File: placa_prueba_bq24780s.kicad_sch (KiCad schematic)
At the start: 1 part, among them U1 BQ24780SRUYR

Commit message: Avances en el esquemático.
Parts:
- added C22: 0.01u, symbol Device:C_Small
- added C3, C4, C5: 0.1u, symbol Device:C_Small
- added C6: 1u, symbol Device:C_Small
- added R20: 100k, symbol Device:R_Small
- added R21: 316k, symbol Device:R_Small
- added R7: 10, symbol Device:R_Small
- added RAC: 10m, symbol Device:R_Small
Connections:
- net at U1.1 (ACN): now also C4.1, C5.2, RAC.2
- net at U1.2 (ACP): now also C3.2, C4.2, RAC.1
- net at U1.21 (ILIM): now also C22.1, R20.1, R21.2
- net at U1.28 (VCC): now also C6.1, R7.2
- new net +12V: R7.1
- new net +3V3: R21.1
- new net GND: C22.2, C3.1, C5.1, C6.2, R20.2

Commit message: Más avances en el esquemático.
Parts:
- added C1: 2.2u, symbol Device:C
- added C10, C11, C12: 0.1u, symbol Device:C_Small
- added C13, C9: 47n, symbol Device:C_Small
- added C18, C7: 10u, symbol Device:C_Small
- added C8: 2.2u, symbol Device:C_Small
- added J2: Conn_01x09_Pin, symbol Connector:Conn_01x09_Pin
- added L1: 3.3u, symbol Device:L_Small
- added Q1, Q2, Q3, Q4, Q5: NMOS, Package_TO_SOT_SMD:TO-252-2, symbol Simulation_SPICE:NMOS
- added R1, R2: 3.9, symbol Device:R_Small
- added R12, R13, R14: 10, symbol Device:R_Small
- added R3: 430k, symbol Device:R_Small
- added R3, R4, R5: 4.02k, symbol Device:R_Small
- added R4: 66.5k, symbol Device:R_Small
- added RSR: 10m, symbol Device:R_Small
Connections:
- net +12V: now also C1.1, Q1.1 (D), R3.1
- net +3V3: now also J2.1 (Pin_1)
- net GND: now also U1.13 (CMPIN), U1.22 (GND), U1.29 (PAD), C10.1, C12.2, C18.2, C7.2, C8.2, Q5.3 (S), R1.2, R2.2, R4.2
- net at C4.1, C5.2, RAC.2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: now also Q2.1 (D)
- net at U1.10 (PROCHOT_N): now also J2.2 (Pin_2)
- net at U1.11 (SDA): now also J2.7 (Pin_7)
- net at U1.12 (SCL): now also J2.6 (Pin_6)
- net at U1.16 (TB_STAT_N): now also J2.9 (Pin_9)
- net at U1.17 (BATSRC): now also R12.1
- net at U1.18 (BATDRV): now also R5.1
- net at U1.19 (SRN): now also R14.2
- net SYS: now reaches C3.2, C4.2, RAC.1, U1.2 (ACP)
- net SYS: now also C18.1, C7.1, Q3.1 (D), Q4.1 (D)
- net at U1.20 (SRP): now also R13.2
- net at U1.23 (LODRV): now also Q5.2 (G)
- net at U1.24 (REGN): now also C8.1
- net at U1.25 (BTST): now also C9.1
- net at U1.26 (HIDRV): now also Q4.2 (G)
- net at U1.27 (PHASE): now also C9.2, L1.1, Q4.3 (S), Q5.1 (D)
- net at U1.3 (CMSRC): now also R4.2
- net at U1.4 (ACDRV): now also R3.2
- net at U1.5 (ACOK): now also J2.8 (Pin_8)
- net ACDET: now reaches U1.6 (ACDET)
- net ACDET: now also R3.2, R4.1
- net at U1.7 (IADP): now also J2.4 (Pin_4)
- net at U1.8 (IDCHG): now also J2.5 (Pin_5)
- net at U1.9 (PMON): now also J2.3 (Pin_3)
- new net: C10.2, C11.1, L1.2, Q3.3 (S), R12.2, R13.1, RSR.1
- new net: C1.2, R1.1, R2.1
- new net: C13.2, Q1.2 (G), Q2.2 (G), R3.1
- new net: C13.1, Q1.3 (S), Q2.3 (S), R4.1
- new net: Q3.2 (G), R5.2
- new net BAT: C11.2, C12.1, R14.1, RSR.2
- no-connect marks 0 -> 1
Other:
- title: (none) -> Placa prueba BQ24780s
- moved on the sheet: C22, C3, C4, C5, C6, R20, R21, R7, RAC, U1

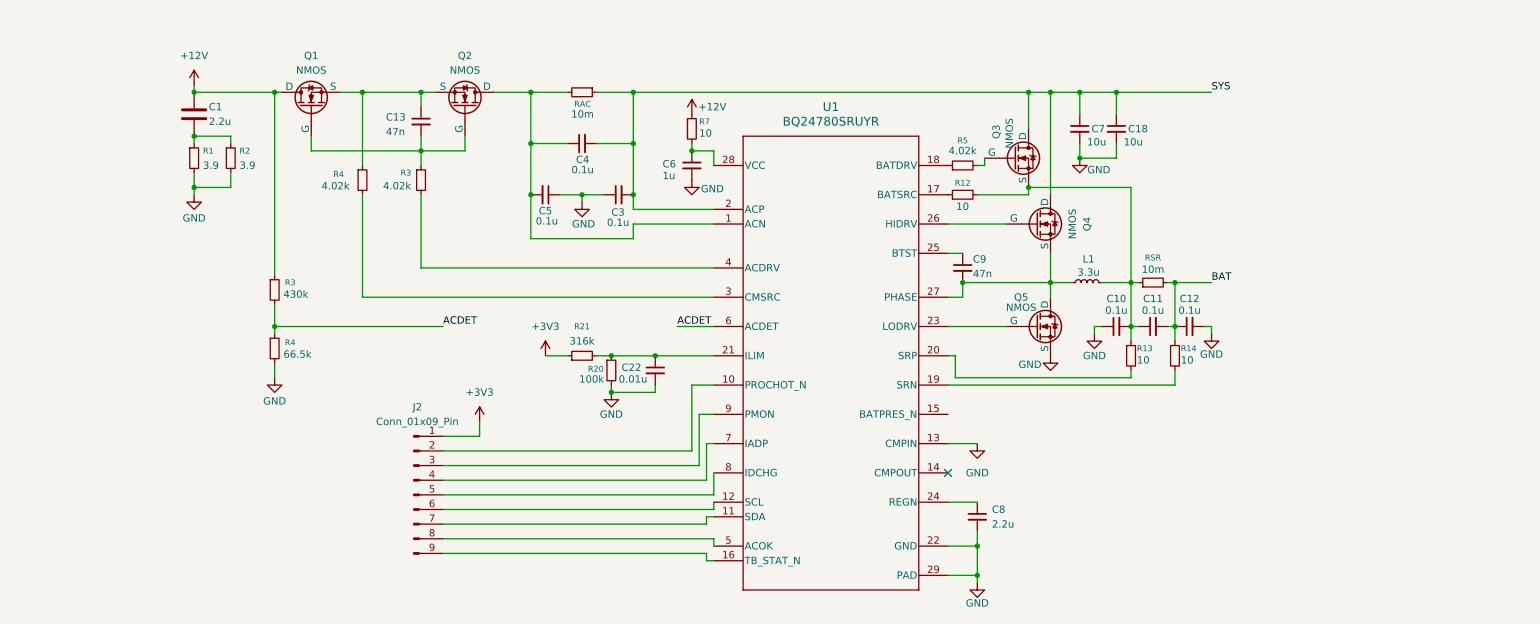
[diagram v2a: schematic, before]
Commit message: Se terminó esquemático y se asignaron footprints.
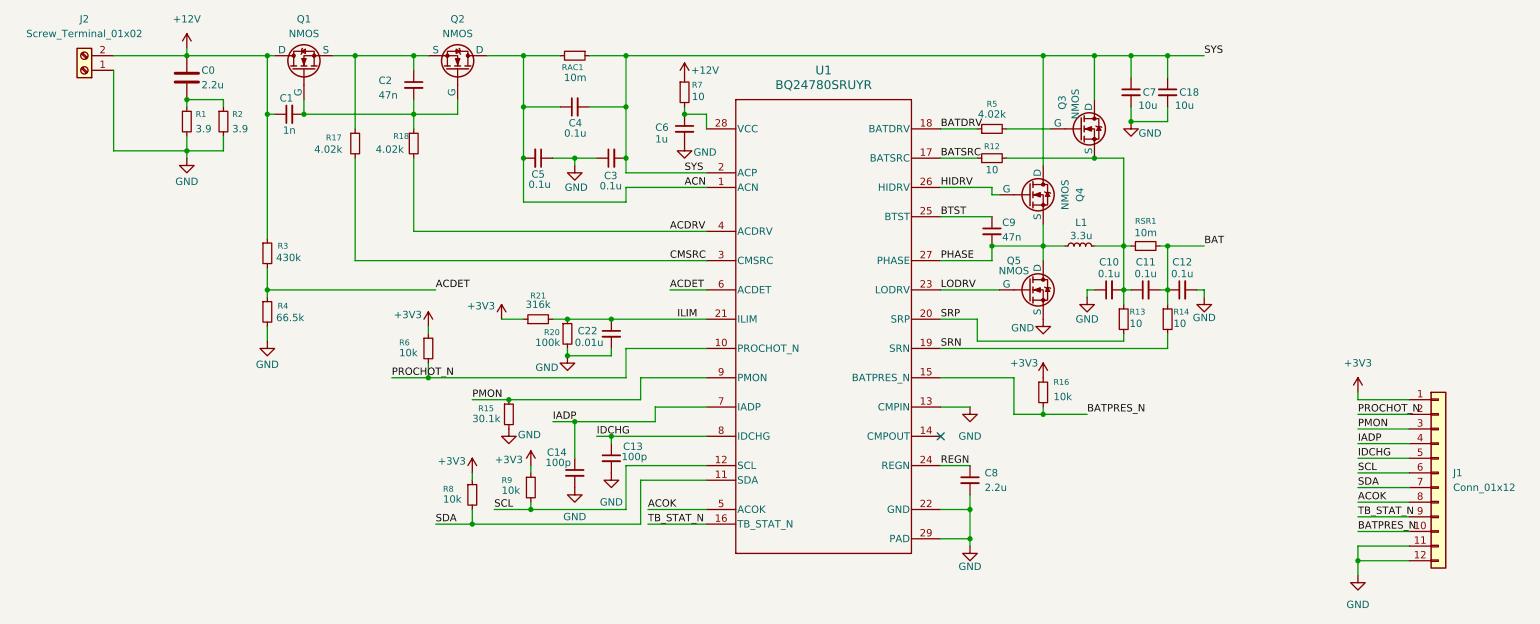
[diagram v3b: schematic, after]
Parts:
- removed J2: Conn_01x09_Pin, symbol Connector:Conn_01x09_Pin
- added C1: 1n, Capacitor_SMD:C_0805_2012Metric, symbol Device:C_Small
- added C13, C14: 100p, Capacitor_SMD:C_0805_2012Metric, symbol Device:C_Small
- added J1: Conn_01x12, Connector_PinHeader_2.54mm:PinHeader_1x12_P2.54mm_Vertical, symbol Connector_Generic:Conn_01x12
- added J2: Screw_Terminal_01x02, TerminalBlock:TerminalBlock_Altech_AK300-2_P5.00mm, symbol Connector:Screw_Terminal_01x02
- added R15: 30.1k, Resistor_SMD:R_1206_3216Metric, symbol Device:R_Small
- added R16, R6, R8, R9: 10k, Resistor_SMD:R_1206_3216Metric, symbol Device:R_Small
- C0: renamed from C1; footprint (none) -> Capacitor_SMD:C_0805_2012Metric
- C10, C11, C12, C18, C22, C3, C4, C5, C6, C7, C8, C9: footprint (none) -> Capacitor_SMD:C_0805_2012Metric
- C2: renamed from C13; footprint (none) -> Capacitor_SMD:C_0805_2012Metric
- L1: footprint (none) -> Inductor_THT:L_Toroid_Vertical_L16.4mm_W7.6mm_P6.60mm_Vishay_TJ3
- R1, R12, R13, R14, R2, R20, R21, R3, R4, R5, R7: footprint (none) -> Resistor_SMD:R_1206_3216Metric
- R17: renamed from R4; footprint (none) -> Resistor_SMD:R_1206_3216Metric
- R18: renamed from R3; footprint (none) -> Resistor_SMD:R_1206_3216Metric
- RAC1: renamed from RAC; footprint (none) -> Resistor_SMD:R_1206_3216Metric
- RSR1: renamed from RSR; footprint (none) -> Resistor_SMD:R_1206_3216Metric
- U1: footprint RUY0028A -> project_pcb_footprints:RUY0028A
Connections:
- net +12V: now also C1.1, J2.2 (Pin_2)
- net +3V3: now also J1.1 (Pin_1), R16.1, R6.1, R8.1, R9.1
- net GND: now also C13.2, C14.2, J1.11 (Pin_11), J1.12 (Pin_12), J2.1 (Pin_1), R15.2
- net ILIM: now reaches C22.1, R20.1, R21.2, U1.21 (ILIM)
- net ACN: now reaches C4.1, C5.2, Q2.1 (D), RAC1.2, U1.1 (ACN)
- net PROCHOT_N: now reaches U1.10 (PROCHOT_N)
- net PROCHOT_N: now also J1.2 (Pin_2), R6.2
- net SDA: now reaches U1.11 (SDA)
- net SDA: now also J1.7 (Pin_7), R8.2
- net SCL: now reaches U1.12 (SCL)
- net SCL: now also J1.6 (Pin_6), R9.2
- net BATPRES_N: now reaches U1.15 (BATPRES_N)
- net BATPRES_N: now also J1.10 (Pin_10), R16.2
- net TB_STAT_N: now reaches U1.16 (TB_STAT_N)
- net TB_STAT_N: now also J1.9 (Pin_9)
- net BATSRC: now reaches R12.1, U1.17 (BATSRC)
- net BATDRV: now reaches R5.1, U1.18 (BATDRV)
- net SRN: now reaches R14.2, U1.19 (SRN)
- net SRP: now reaches R13.2, U1.20 (SRP)
- net LODRV: now reaches Q5.2 (G), U1.23 (LODRV)
- net REGN: now reaches C8.1, U1.24 (REGN)
- net BTST: now reaches C9.1, U1.25 (BTST)
- net HIDRV: now reaches Q4.2 (G), U1.26 (HIDRV)
- net PHASE: now reaches C9.2, L1.1, Q4.3 (S), Q5.1 (D), U1.27 (PHASE)
- net CMSRC: now reaches R17.2, U1.3 (CMSRC)
- net ACDRV: now reaches R18.2, U1.4 (ACDRV)
- net ACOK: now reaches U1.5 (ACOK)
- net ACOK: now also J1.8 (Pin_8)
- net IADP: now reaches U1.7 (IADP)
- net IADP: now also C14.1, J1.4 (Pin_4)
- net IDCHG: now reaches U1.8 (IDCHG)
- net IDCHG: now also C13.1, J1.5 (Pin_5)
- net PMON: now reaches U1.9 (PMON)
- net PMON: now also J1.3 (Pin_3), R15.1
- net at C2.2, Q1.2 (G), Q2.2 (G)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: now also C1.2
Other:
- moved on the sheet: C0, C10, C11, C12, C18, C2, C22, C3, C4, C5, C6, C7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

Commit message: Más avances.
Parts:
- removed Q1, Q2, Q3, Q4, Q5: NMOS, Package_TO_SOT_SMD:TO-252-2, symbol Simulation_SPICE:NMOS
- added Q1, Q2, Q3, Q4, Q5: CSD17308Q3, DQG0008A, symbol CSD17308Q3:CSD17308Q3
- added U2: TPS3898ADRYT, DRY6, symbol TPS3898ADRY:TPS3898ADRYT
- U1: footprint project_pcb_footprints:RUY0028A -> BQ24780S:RUY0028A
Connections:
- net GND: now also Q5.3 (S)
- net PHASE: now also Q4.3 (S)
- net at C10.2, C11.1, L1.2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: now also Q3.3 (S)
- net at C2.1, R17.1: now also Q1.3 (S), Q2.3 (S)
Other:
- moved on the sheet: C0, C1, C10, C11, C12, C13, C14, C18, C2, C22, C3, C4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

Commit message: Más correcciones y avances.
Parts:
- removed U2: TPS3898ADRYT, DRY6, symbol TPS3898ADRY:TPS3898ADRYT
- added C15: 22u, Capacitor_SMD:C_0805_2012Metric, symbol Device:C_Small
- added C16, C17: 10u, Capacitor_SMD:C_0805_2012Metric, symbol Device:C_Small
- added C27: 0.01u, symbol Device:C_Small
- added J3, J4: Screw_Terminal_01x02, TerminalBlock:TerminalBlock_Altech_AK300-2_P5.00mm, symbol Connector:Screw_Terminal_01x02
- Q1, Q2, Q3, Q4, Q5: footprint DQG0008A -> CSD17308Q3:DQG0008A
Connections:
- net BAT: now also C16.1, C17.1, J4.2 (Pin_2)
- net GND: now also C15.2, C16.2, C17.2, J3.1 (Pin_1), J4.1 (Pin_1)
- net SYS: now also C15.1, J3.2 (Pin_2)
- net VCC: now reaches C6.1, R7.2, U1.28 (VCC)
- net at C10.2, C11.1, L1.2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: now also C27.2
- net at R5.2: now also C27.1
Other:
- moved on the sheet: C0, C1, C10, C11, C12, C13, C14, C18, C2, C22, C3, C4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

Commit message: Se agregaron simulaciones de LTSpice.
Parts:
- removed J2: Screw_Terminal_01x02, TerminalBlock:TerminalBlock_Altech_AK300-2_P5.00mm, symbol Connector:Screw_Terminal_01x02
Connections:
- net SYS: now also C27.1, R5.2
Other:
- note added: "MODULOS DE CARGA"
- moved on the sheet: C0, C1, C10, C11, C12, C13, C14, C15, C16, C17, C18, C2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

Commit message: Simulaciones y avances en el esquemático.
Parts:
- added C19: 1n, Capacitor_SMD:C_0805_2012Metric, symbol Device:C_Small
- added F1: 3F.1000212000R1N, Fuse:Fuse_2920_7451Metric, symbol Device:Fuse_Small
- added Q6: 2N2222A, Package_TO_SOT_THT:TO-92, symbol Simulation_SPICE:NPN
- added Q7: TIP36C, Package_TO_SOT_THT:TO-247-3_Vertical, symbol Simulation_SPICE:PNP
- added R10: 100, Resistor_SMD:R_1206_3216Metric, symbol Device:R_Small
- added R11: 1k, Resistor_SMD:R_1206_3216Metric, symbol Device:R_Small
- added R19: 100m, Resistor_SMD:R_1206_3216Metric, symbol Device:R_Small
- added R22: 9.1k, Resistor_SMD:R_1206_3216Metric, symbol Device:R_Small
- added R23: 10k, Resistor_SMD:R_1206_3216Metric, symbol Device:R_Small
- added R24: 91k, Resistor_SMD:R_1206_3216Metric, symbol Device:R_Small
- added U2: STM32WB55RGVx, Package_DFN_QFN:QFN-68-1EP_8x8mm_P0.4mm_EP6.4x6.4mm, symbol MCU_ST_STM32WB:STM32WB55RGVx
- added U3: LM358, Package_SO:SOIC-8-1EP_3.9x4.9mm_P1.27mm_EP2.29x3mm, symbol Amplifier_Operational:LM358
- C27: footprint (none) -> Capacitor_SMD:C_0805_2012Metric
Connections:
- net GND: now also R19.2, R23.2
- net SYS: now also F1.2
- new net: Q6.3 (E), Q7.1 (C), R19.1, R22.2
- new net: Q6.1 (C), Q7.2 (B), R10.2
- new net: F1.1, Q7.3 (E), R10.1
- new net: C19.2, R22.1, U3.2 (-)
- new net: R23.1, R24.2, U3.3 (+)
- new net: C19.1, R11.1, U3.1
- new net: Q6.2 (B), R11.2
- new net DAC1: R24.1
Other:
- note added: "MODULOS CARGA"
- note added: "MODULOS DESCARGA"
- note removed: "MODULOS DE CARGA"
- moved on the sheet: C0, C1, C10, C11, C12, C13, C14, C15, C16, C17, C18, C2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
